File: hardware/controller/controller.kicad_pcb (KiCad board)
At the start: 2 copper layers, 100 x 70 mm, 210 parts, among them J1 USB_C_Receptacle_USB2.0_14P, J10 Conn_01x01, J11 Conn_01x01, J12 Conn_01x01, J13 Conn_02x03_Odd_Even, J2 IDC-10, J3 USB_C_Receptacle_USB2.0_14P, J4 XT-60, J5 Conn_01x07, J6 Conn_01x01, J7 Conn_01x01, J8 Conn_01x01, J9 Conn_02x03_Odd_Even, Q1 SUD50P04-08, Q10 AOD66406, Q11 AOD66406, Q12 AOD66406, Q13 AOD66406, Q2 AOD66406, Q3 AOD66406, Q4 AOD66406, Q5 AOD66406, Q6 AOD66406, Q7 AOD66406, Q8 AOD66406, Q9 AOD66406, SW1 SW_Push, SW2 SW_Push, SW3 SW_Push, SW4 SW_Push, SW5 SW_SPST, U1 USBLC6-2SC6, U10 LMV331, U11 IR2101, U12 LMV331, U13 IR2101, U14 LMV331, U15 IR2101, U16 LMV331, U17 IR2101, U18 LMV331, U19 IR2101, U2 ESP32-C3-WROOM-02, U20 LMV331, U3 STM32U535RET6, U4 nRF24L01+ 2.4Gz Mini SMD, U5 USBLC6-2SC6, U6 LM1117MP-3.3, U7 LV14340, U8 MPU-6050, U9 IR2101, Y1 8MHz

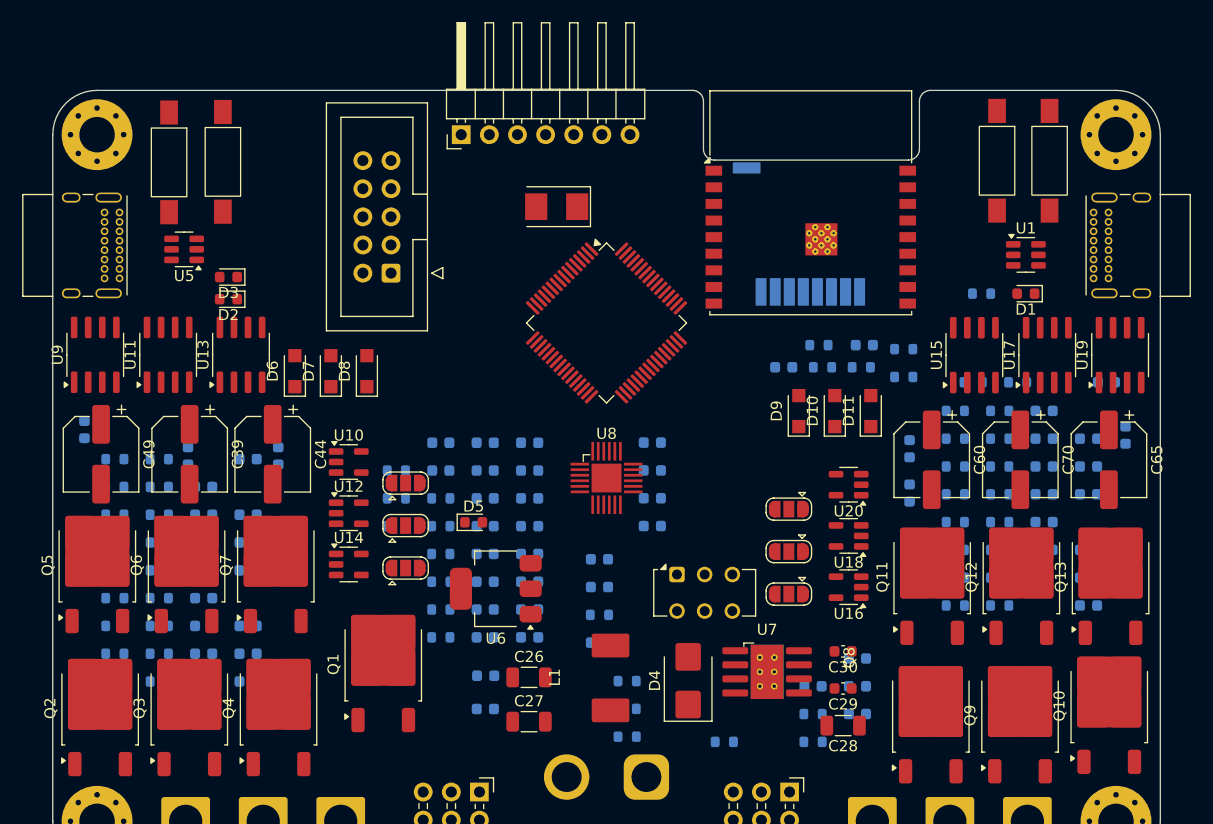
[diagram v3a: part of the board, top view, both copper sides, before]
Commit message: back to LM2105, remove USB-C from STM
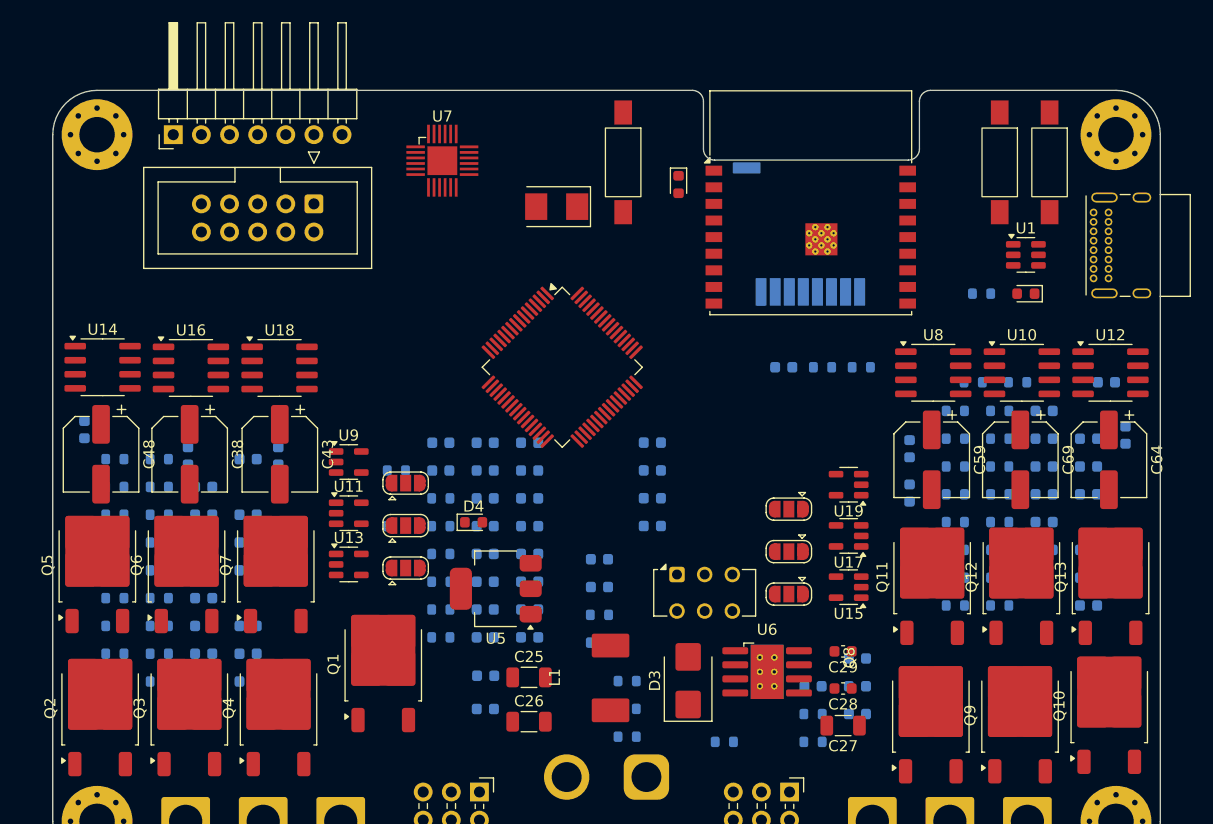
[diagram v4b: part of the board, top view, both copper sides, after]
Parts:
- removed the C15 at (173.3, 73.0)
- removed D10, D11, D6, D7, D8, D9: 1N5819HW-7-F, Diode_SMD:Nexperia_CFP3_SOD-123W
- removed the D2 at (115.9, 68.9)
- removed the J3 at (106.0, 61.0)
- removed the R10 at (131.0, 86.8)
- removed the R12 at (176.8, 73.4)
- removed the R13 at (176.8, 75.9)
- removed the R9 at (169.2, 73.0)
- removed the SW3 at (110.5, 56.5)
- removed the U11 at (110.4, 73.9)
- removed the U13 at (117.0, 73.9)
- removed the U15 at (183.2, 73.9)
- removed the U17 at (189.8, 73.9)
- removed the U19 at (196.4, 73.9)
- removed the U5 at (111.9, 64.4)
- removed the U9 at (103.8, 73.9)
- added U10: LM2105D, Package_SO:SOIC-8_3.9x4.9mm_P1.27mm, F.Cu at (187.5, 75.5)
- added U12: LM2105D, Package_SO:SOIC-8_3.9x4.9mm_P1.27mm, F.Cu at (195.5, 75.5)
- added U14: LM2105D, Package_SO:SOIC-8_3.9x4.9mm_P1.27mm, F.Cu at (104.5, 75.0)
- added U16: LM2105D, Package_SO:SOIC-8_3.9x4.9mm_P1.27mm, F.Cu at (112.5, 75.1)
- added U18: LM2105D, Package_SO:SOIC-8_3.9x4.9mm_P1.27mm, F.Cu at (120.5, 75.1)
- added U8: LM2105D, Package_SO:SOIC-8_3.9x4.9mm_P1.27mm, F.Cu at (179.5, 75.5)
- moved SW3 70.1 mm to (185.5, 56.5)
- moved D2 41.5 mm to (156.5, 58.5), turned to -90 degrees
- moved SW1 33.8 mm to (151.5, 56.5)
- moved U7 32.3 mm to (135.2, 56.4)
- moved J4 26.0 mm to (110.9, 54.0)
- moved J2 9.36 mm to (123.6, 60.2), turned to -90 degrees
- moved U3 5.66 mm to (146.0, 75.0)
- moved C43 0.64 mm to (120.5, 82.9)
- moved SW2 0.15 mm to (190.0, 56.5)
- renumbered C5 to C1, C16 to C15, C17 to C16, C18 to C17, C19 to C18, C20 to C19, C6 to C2, C21 to C20, C22 to C21, C23 to C22, C24 to C23, C25 to C24, C26 to C25, C27 to C26, C28 to C27, C29 to C28, C30 to C29, C1 to C3, C31 to C30, C32 to C31, C33 to C32, C34 to C33, C35 to C34, C36 to C35, C37 to C36, C38 to C37, C39 to C38, C40 to C39, C2 to C4, C41 to C40, C42 to C41, C43 to C42, C44 to C43, C45 to C44, C46 to C45, C47 to C46, C48 to C47, C49 to C48, C50 to C49, C3 to C5, C51 to C50, C52 to C51, C53 to C52, C54 to C53, C55 to C54, C56 to C55, C57 to C56, C58 to C57, C59 to C58, C60 to C59, C4 to C6, C61 to C60, C62 to C61, C63 to C62, C64 to C63, C65 to C64, C66 to C65, C67 to C66, C68 to C67, C69 to C68, C70 to C69, C71 to C70, C72 to C71, C73 to C72, C74 to C73, C75 to C74, C76 to C75, C77 to C76, D3 to D2, D4 to D3, D5 to D4, J11 to J10, J12 to J11, J13 to J12, J4 to J3, J5 to J4, J6 to J5, J7 to J6, J8 to J7, J9 to J8, J10 to J9, R14 to R10, R15 to R11, R16 to R12, R17 to R13, R18 to R14, R19 to R15, R20 to R16, R21 to R17, R22 to R18, R23 to R19, R24 to R20, R25 to R21, R26 to R22, R27 to R23, R28 to R24, R29 to R25, R30 to R26, R31 to R27, R32 to R28, R33 to R29, R34 to R30, R35 to R31, R36 to R32, R37 to R33, R38 to R34, R39 to R35, R40 to R36, R41 to R37, R42 to R38, R43 to R39, R44 to R40, R45 to R41, R46 to R42, R47 to R43, R48 to R44, R49 to R45, R50 to R46, R51 to R47, R52 to R48, R53 to R49, R54 to R50, R55 to R51, R56 to R52, R57 to R53, R58 to R54, R59 to R55, R11 to R9, SW4 to SW3, SW5 to SW4, U12 to U11, U14 to U13, U16 to U15, U18 to U17, U20 to U19, U6 to U5, U7 to U6, U8 to U7, U10 to U9
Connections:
- net /microcontroller/LED_B renamed /microcontroller/STM_LED
- U3 pad 25: unconnected-(U3-PC5-Pad25) -> FLOW_CS
- U3 pad 28: FLOW_CS -> MOTOR1_BEMF_W
- U3 pad 33: MOTOR1_BEMF_W -> unconnected-(U3-PB12-Pad33)
- U3 pad 44: /microcontroller/STM_USB_D- -> unconnected-(U3-PA11-Pad44)
- U3 pad 45: /microcontroller/STM_USB_D+ -> unconnected-(U3-PA12-Pad45)
- U3 pad 56: /microcontroller/LED_G -> unconnected-(U3-PB4-Pad56)
- U3 pad 60: /microcontroller/STM_BOOT0 -> GND

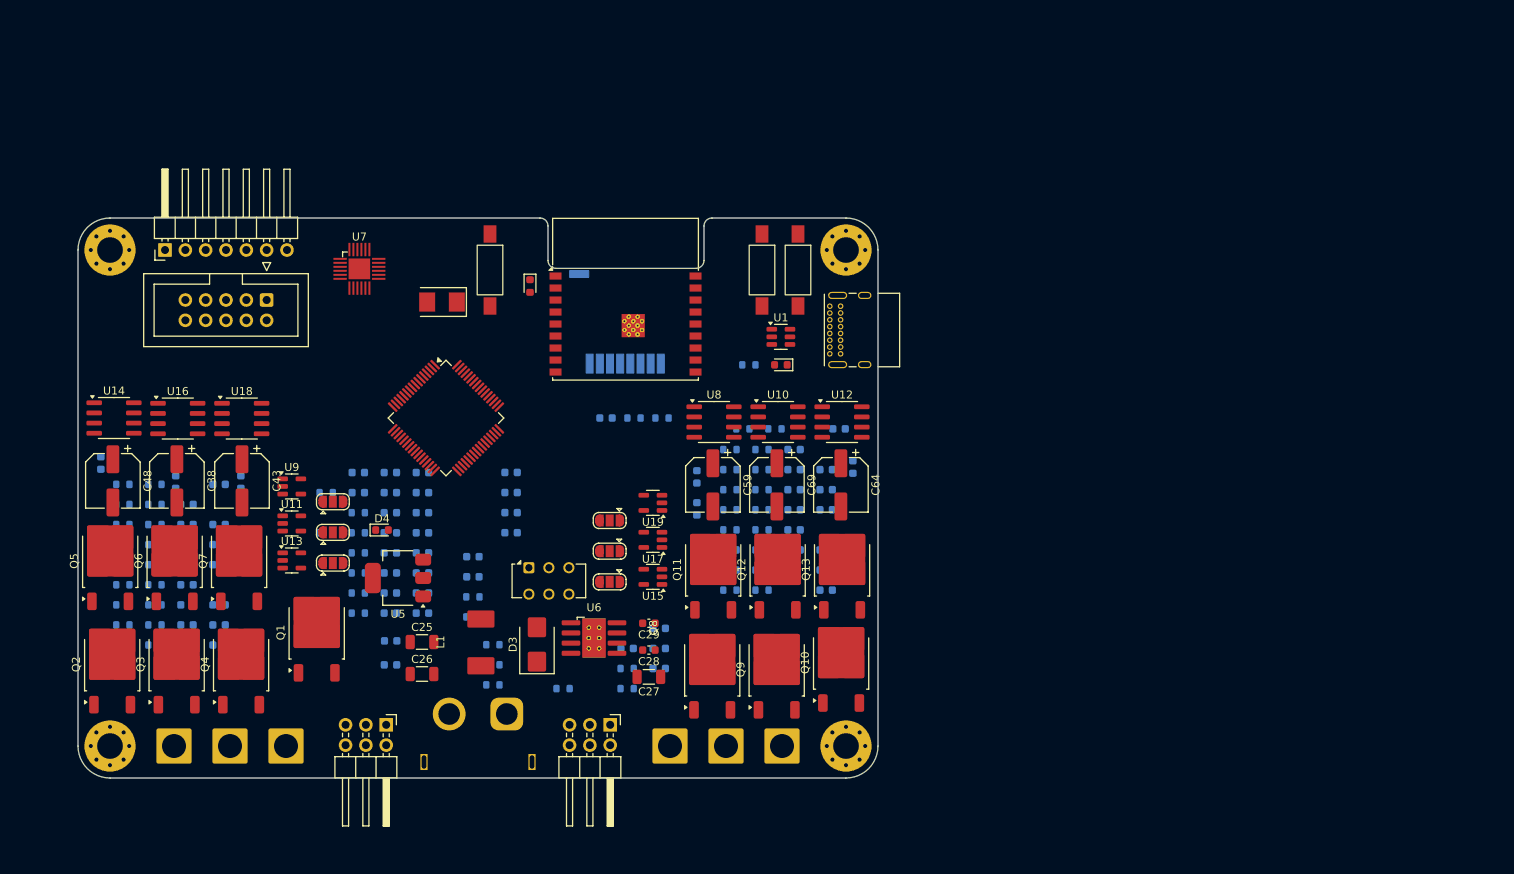
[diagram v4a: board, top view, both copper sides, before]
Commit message: first real layout, change comps to MCP6541
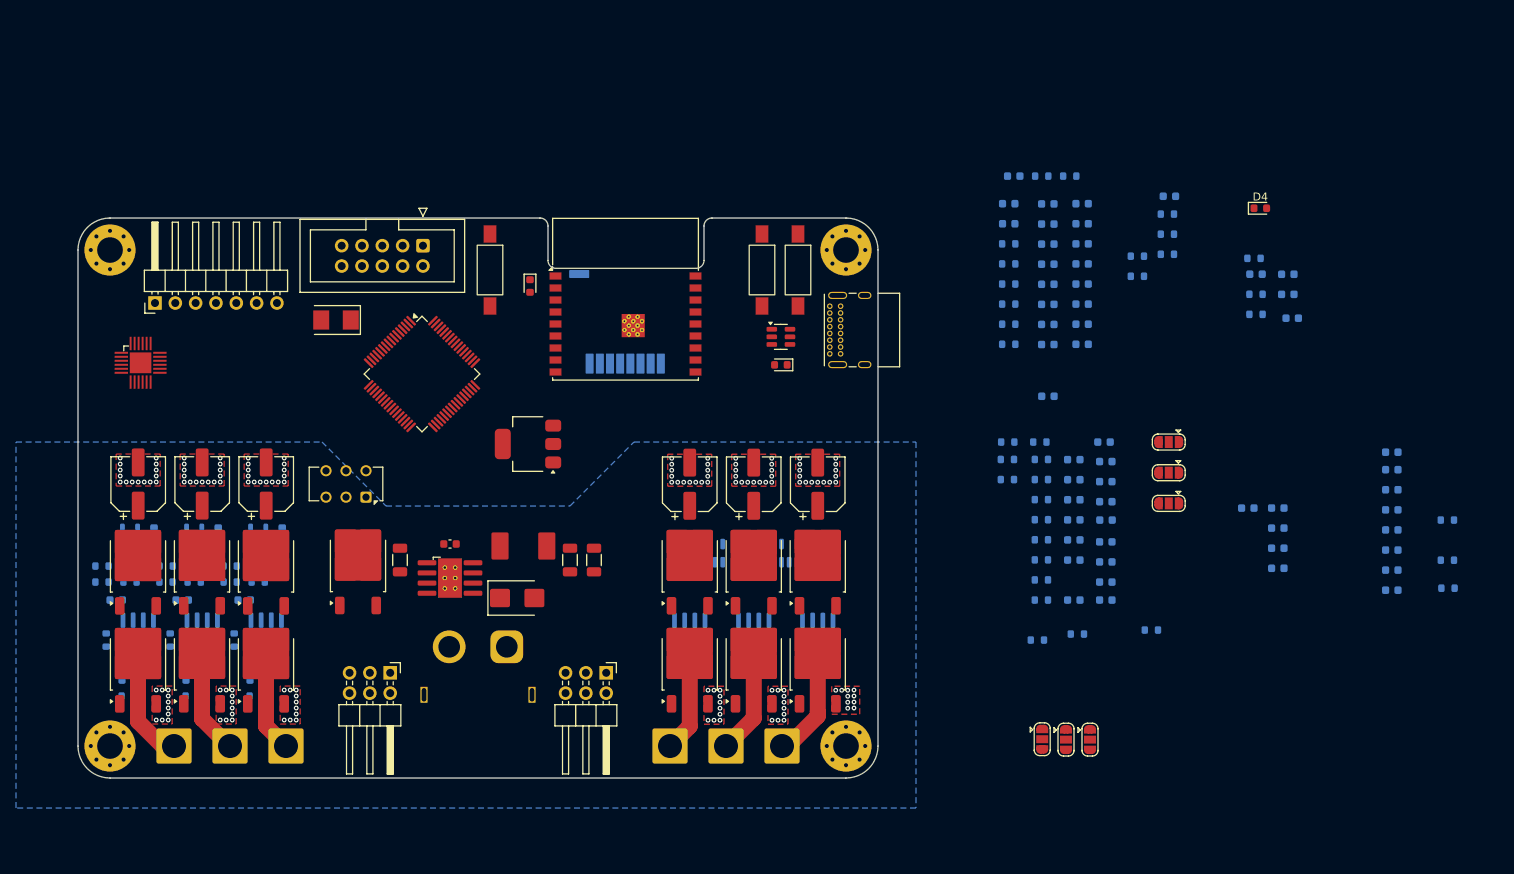
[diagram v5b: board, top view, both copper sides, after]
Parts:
- removed R50, R52: 47k, Resistor_SMD:R_0603_1608Metric
- removed R51, R55: 100, Resistor_SMD:R_0603_1608Metric
- removed R53, R54: 10k, Resistor_SMD:R_0603_1608Metric
- C20: moved to F.Cu
- C28, C29, U10, U12, U14, U16, U18, U8: moved to B.Cu
- C36, C41, C46, C57, C62, C67: value 1u/50V -> 100n/50V
- R23, R35, R40, R46: value 10k -> 100
- R24, R26, R42: value 100 -> 47k
- R25, R29, R34: value 47k -> 100
- R30, R36, R41: value 10k -> 47k
- R33, R37: value 100 -> 10k
- R43: value 47k -> 10k
- U11, U13, U15, U17, U19, U9: value LMV331 -> MCP6541; moved to B.Cu
- moved C51 150.8 mm to (264.2, 81.5)
- moved C52 150.8 mm to (264.2, 84.0)
- moved C53 150.8 mm to (264.2, 86.5)
- moved C54 150.8 mm to (264.2, 89.0)
- moved C55 150.8 mm to (264.2, 91.5)
- moved C56 150.8 mm to (264.2, 94.0)
- moved C57 150.8 mm to (264.2, 96.5)
- moved C50 143.9 mm to (264.2, 79.3), turned to 180 degrees
- moved R8 140.2 mm to (271.2, 87.8)
- moved R9 140.2 mm to (271.2, 92.8)
- moved R37 128.6 mm to (234.2, 101.5)
- moved R36 119.3 mm to (224.9, 102.0)
- moved D4 116.9 mm to (247.8, 48.8)
- moved R35 114.4 mm to (219.9, 102.8)
- moved R17 101.7 mm to (247.0, 55.0)
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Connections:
- Q10 pad 1: VBUS -> Net-(Q10-G)
- Q10 pad 2: Net-(Q10-G) -> VBUS
- Q11 pad 1: /hog2/PHASE_V -> Net-(Q11-G)
- Q11 pad 2: Net-(Q11-G) -> /hog2/PHASE_V
- Q12 pad 1: VBUS -> Net-(Q12-G)
- Q12 pad 2: Net-(Q12-G) -> VBUS
- Q13 pad 1: /hog2/PHASE_W -> Net-(Q13-G)
- Q13 pad 2: Net-(Q13-G) -> /hog2/PHASE_W
- Q2 pad 1: VBUS -> Net-(Q2-G)
- Q2 pad 2: Net-(Q2-G) -> VBUS
- Q3 pad 1: /hog1/PHASE_U -> Net-(Q3-G)
- Q3 pad 2: Net-(Q3-G) -> /hog1/PHASE_U
- Q4 pad 1: VBUS -> Net-(Q4-G)
- Q4 pad 2: Net-(Q4-G) -> VBUS
- Q5 pad 1: /hog1/PHASE_V -> Net-(Q5-G)
- Q5 pad 2: Net-(Q5-G) -> /hog1/PHASE_V
- Q6 pad 1: VBUS -> Net-(Q6-G)
- Q6 pad 2: Net-(Q6-G) -> VBUS
- Q7 pad 1: /hog1/PHASE_W -> Net-(Q7-G)
- Q7 pad 2: Net-(Q7-G) -> /hog1/PHASE_W
- Q8 pad 1: VBUS -> Net-(Q8-G)
- Q8 pad 2: Net-(Q8-G) -> VBUS
- Q9 pad 1: /hog2/PHASE_U -> Net-(Q9-G)
- Q9 pad 2: Net-(Q9-G) -> /hog2/PHASE_U
- R22 pad 1: +3.3V -> /hog1/BEMF_U
- R22 pad 2: Net-(JP1-B) -> GND
- R23 pad 1: /hog1/BEMF_U -> Net-(U8-GL)
- R23 pad 2: GND -> Net-(Q3-G)
- R24 pad 1: Net-(U8-GL) -> /hog1/BEMF_U
- R24 pad 2: Net-(Q3-G) -> /hog1/BEMF_ZERO
- R25 pad 1: /hog1/BEMF_U -> Net-(U10-GH)
- R25 pad 2: /hog1/BEMF_ZERO -> Net-(Q4-G)
- R26 pad 1: Net-(U10-GH) -> /hog1/PHASE_V
- R26 pad 2: Net-(Q4-G) -> /hog1/BEMF_V
- R27 pad 1: /hog1/PHASE_V -> /hog1/BEMF_V
- R27 pad 2: /hog1/BEMF_V -> /hog1/BEMF_ZERO
- R28 pad 1: +3.3V -> /hog1/BEMF_V
- R28 pad 2: Net-(JP2-B) -> GND
- R29 pad 1: /hog1/BEMF_V -> Net-(U10-GL)
- R29 pad 2: /hog1/BEMF_ZERO -> Net-(Q5-G)
- R30 pad 1: /hog1/BEMF_V -> /hog1/BEMF_W
- R30 pad 2: GND -> /hog1/BEMF_ZERO
- R31 pad 1: Net-(U10-GL) -> Net-(U12-GH)
- R31 pad 2: Net-(Q5-G) -> Net-(Q6-G)
- R32 pad 1: /hog1/BEMF_W -> /hog1/PHASE_W
- R32 pad 2: /hog1/BEMF_ZERO -> /hog1/BEMF_W
- R33 pad 1: Net-(U12-GH) -> /hog1/BEMF_W
- R33 pad 2: Net-(Q6-G) -> GND
- R34 pad 1: /hog1/PHASE_W -> Net-(U12-GL)
- R34 pad 2: /hog1/BEMF_W -> Net-(Q7-G)
- R35 pad 1: +3.3V -> Net-(U14-GH)
- R35 pad 2: Net-(JP3-B) -> Net-(Q8-G)
- R36 pad 1: /hog1/BEMF_W -> /hog2/PHASE_U
- R36 pad 2: GND -> /hog2/BEMF_U
- R37 pad 1: Net-(U12-GL) -> /hog2/BEMF_U
- R37 pad 2: Net-(Q7-G) -> GND
- R38 pad 1: Net-(U14-GH) -> Net-(U14-GL)
- R38 pad 2: Net-(Q8-G) -> Net-(Q9-G)
- R39 pad 1: /hog2/PHASE_U -> /hog2/BEMF_U
- R39 pad 2: /hog2/BEMF_U -> /hog2/BEMF_ZERO
- R40 pad 1: +3.3V -> Net-(U16-GH)
- R40 pad 2: Net-(JP4-B) -> Net-(Q10-G)
- R41 pad 1: /hog2/BEMF_U -> /hog2/PHASE_V
- R41 pad 2: GND -> /hog2/BEMF_V
- R42 pad 1: Net-(U14-GL) -> /hog2/BEMF_V
- R42 pad 2: Net-(Q9-G) -> /hog2/BEMF_ZERO
- R43 pad 1: /hog2/BEMF_U -> /hog2/BEMF_V
- R43 pad 2: /hog2/BEMF_ZERO -> GND
- R44 pad 1: Net-(U16-GH) -> Net-(U16-GL)
- R44 pad 2: Net-(Q10-G) -> Net-(Q11-G)
- R45 pad 1: /hog2/PHASE_V -> /hog2/BEMF_W
- R45 pad 2: /hog2/BEMF_V -> /hog2/BEMF_ZERO
- R46 pad 1: +3.3V -> Net-(U18-GH)
- R46 pad 2: Net-(JP5-B) -> Net-(Q12-G)
- R47 pad 1: /hog2/BEMF_V -> /hog2/PHASE_W
- R47 pad 2: /hog2/BEMF_ZERO -> /hog2/BEMF_W
- R48 pad 1: /hog2/BEMF_V -> /hog2/BEMF_W
- R49 pad 1: Net-(U16-GL) -> Net-(U18-GL)
- R49 pad 2: Net-(Q11-G) -> Net-(Q13-G)
- U11 pad 1: /hog1/BEMF_V -> Net-(JP2-B)
- U11 pad 3: /hog1/BEMF_ZERO -> /hog1/BEMF_V
- U11 pad 4: Net-(JP2-B) -> /hog1/BEMF_ZERO
- U13 pad 1: /hog1/BEMF_W -> Net-(JP3-B)
- U13 pad 3: /hog1/BEMF_ZERO -> /hog1/BEMF_W
- U13 pad 4: Net-(JP3-B) -> /hog1/BEMF_ZERO
- U15 pad 1: /hog2/BEMF_U -> Net-(JP4-B)
- U15 pad 3: /hog2/BEMF_ZERO -> /hog2/BEMF_U
- U15 pad 4: Net-(JP4-B) -> /hog2/BEMF_ZERO
- U17 pad 1: /hog2/BEMF_V -> Net-(JP5-B)
- U17 pad 3: /hog2/BEMF_ZERO -> /hog2/BEMF_V
- U17 pad 4: Net-(JP5-B) -> /hog2/BEMF_ZERO
- U19 pad 1: /hog2/BEMF_W -> Net-(JP6-B)
- U19 pad 3: /hog2/BEMF_ZERO -> /hog2/BEMF_W
- U19 pad 4: Net-(JP6-B) -> /hog2/BEMF_ZERO
- U9 pad 1: /hog1/BEMF_U -> Net-(JP1-B)
- U9 pad 3: /hog1/BEMF_ZERO -> /hog1/BEMF_U
- U9 pad 4: Net-(JP1-B) -> /hog1/BEMF_ZERO
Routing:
- net /hog1/PHASE_U: track 0.00 -> 14.3 mm
- net /hog2/PHASE_W: track 0.00 -> 13.9 mm
- net /hog1/PHASE_V: track 0.00 -> 13.1 mm
- net /hog2/PHASE_V: track 0.00 -> 13.0 mm
- net /hog1/PHASE_W: track 0.00 -> 12.6 mm
- net /hog2/PHASE_U: track 0.00 -> 12.6 mm
- net GND: vias 0 -> 150
- added copper zone on In1.Cu, net +3.3V
- added copper zone on B.Cu, net GND
- added copper zone on F.Cu, net GND
- added copper zone on In1.Cu, net GND
- added copper zone on In2.Cu, net GND
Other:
- copper layers 2 -> 4

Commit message: full layout, edge power switch
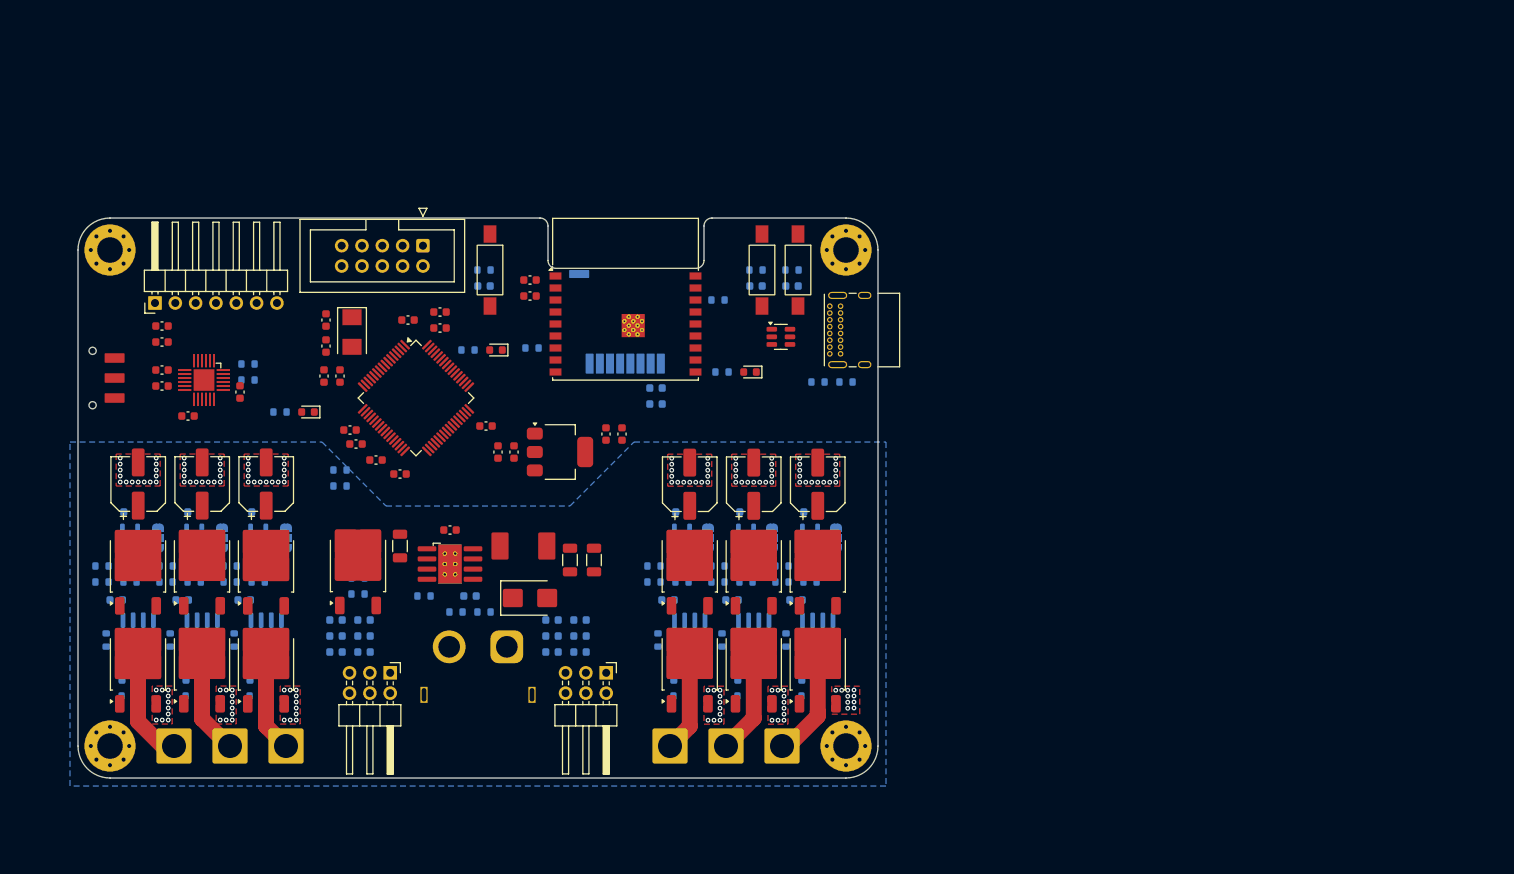
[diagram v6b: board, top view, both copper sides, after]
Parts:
- removed the C2 at (225.5, 65.8)
- added C11: 100n, Capacitor_SMD:C_0603_1608Metric, F.Cu at (151.0, 76.0)
- C1: renamed from C6; moved to F.Cu
- C10: renamed from C1; moved to F.Cu
- C13, C14, C19, C21, C22, C23, C24, C29, C30, C31, C32, C33, C34: moved to F.Cu
- C18: renamed from C16; moved to F.Cu
- C2: renamed from C5; moved to F.Cu
- C3: renamed from C4; moved to F.Cu
- C4: renamed from C3; moved to F.Cu
- C5: renamed from C8; moved to F.Cu
- C6: renamed from C9; moved to F.Cu
- C8: renamed from C11; moved to F.Cu
- C9: renamed from C12; moved to F.Cu
- JP1, JP2, JP3, JP4, JP5, JP6: moved to B.Cu
- SW4: footprint Button_Switch_THT:SW_CK_JS202011CQN_DPDT_Straight -> hogger2:JS102011SAQN
- moved C32 141.7 mm to (110.5, 63.5), turned to 0 degrees
- moved C31 141.0 mm to (110.5, 65.5), turned to 0 degrees
- moved C33 140.9 mm to (110.5, 71.0)
- moved C29 136.8 mm to (110.5, 69.0), turned to 180 degrees
- moved C30 134.7 mm to (113.8, 74.8)
- moved C53 133.2 mm to (132.2, 104.2), turned to 0 degrees
- moved C54 132.6 mm to (132.2, 102.2), turned to 0 degrees
- moved C55 132.3 mm to (132.2, 100.2), turned to 0 degrees
- moved C34 131.6 mm to (120.2, 71.8), turned to -90 degrees
- moved C50 130.2 mm to (135.8, 100.2)
- moved C51 130.1 mm to (135.8, 102.2)
- moved C52 130.1 mm to (135.8, 104.2)
- moved R9 125.2 mm to (148.8, 66.5), turned to 0 degrees
- moved R17 123.3 mm to (125.2, 74.2), turned to 0 degrees
- moved D4 121.7 mm to (128.8, 74.2), turned to 180 degrees
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- renumbered C7 to C12, C17 to C16, C18 to C17, C10 to C7, R4 to R3, R3 to R4, SW2 to SW1, SW1 to SW2
